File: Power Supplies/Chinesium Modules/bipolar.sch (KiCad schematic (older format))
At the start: 15 parts

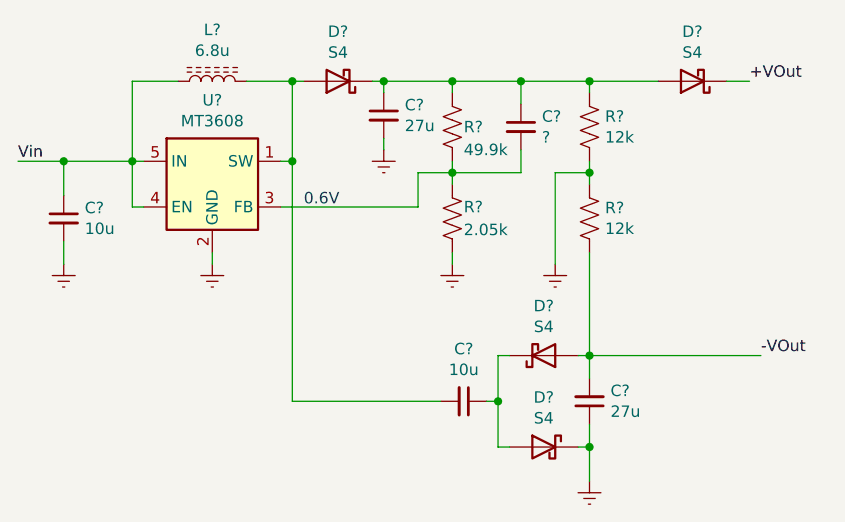
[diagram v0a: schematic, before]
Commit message: update voltage feedback
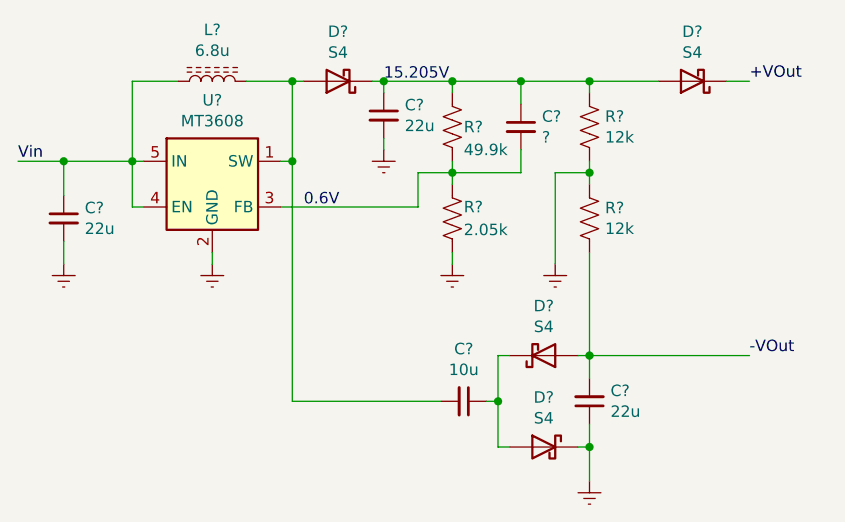
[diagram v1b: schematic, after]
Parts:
- C?: value 10u -> 22u
- C? (x2): value 27u -> 22u
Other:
- note added: "15.205V"
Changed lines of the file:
@@
 P 3200 4650
 F 0 "C?" H 3292 4696 50  0000 L CNN
-F 1 "10u" H 3292 4605 50  0000 L CNN
+F 1 "22u" H 3292 4605 50  0000 L CNN
 F 2 "" H 3200 4650 50  0001 C CNN
 F 3 "~" H 3200 4650 50  0001 C CNN
@@
 P 4600 4200
 F 0 "C?" H 4692 4246 50  0000 L CNN
-F 1 "27u" H 4692 4155 50  0000 L CNN
+F 1 "22u" H 4692 4155 50  0000 L CNN
 F 2 "" H 4600 4200 50  0001 C CNN
 F 3 "~" H 4600 4200 50  0001 C CNN
@@
 P 5500 5450
 F 0 "C?" H 5408 5404 50  0000 R CNN
-F 1 "27u" H 5408 5495 50  0000 R CNN
+F 1 "22u" H 5408 5495 50  0000 R CNN
 F 2 "" H 5500 5450 50  0001 C CNN
 F 3 "~" H 5500 5450 50  0001 C CNN
@@
 Connection ~ 4200 4400
 Connection ~ 5500 5250
-Text Label 6250 5250 0    50   ~ 0
+Text Label 6200 5250 0    50   ~ 0
 -VOut
 Wire Wire Line
-	5500 5250 6250 5250
+	5500 5250 6200 5250
 Wire Wire Line
 	4200 5450 4850 5450
@@
 Text Notes 4250 4600 0    50   ~ 0
 0.6V
+Text Notes 4600 4050 0    50   ~ 0
+15.205V
 $EndSCHEMATC
